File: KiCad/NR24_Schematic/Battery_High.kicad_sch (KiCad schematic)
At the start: 9 parts

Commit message: Back at it
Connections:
- net State_of_Chrg_ANLG: now reaches U?.11 (State_of_Charge(0-5V))
- net Disch_Crnt_Lmt_ANLG: now reaches U?.14 (Discharge_Current_Lim(0-5V))
- net STDWN CT: no longer names the net of U?.15 (Multi_Purpose_Input)
- net STDWN CT: no longer RL1.7
- new net Into Battery AIR Loop: RL1.7
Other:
- note added: "discharge Enable on can"
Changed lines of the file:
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@@
+    (stroke (width 0) (type default))
+  )
+  (wire (pts (xy 118.11 158.75) (xy 81.28 158.75))
     (stroke (width 0) (type default))
   )
@@
     (stroke (width 0) (type default))
   )
+  (wire (pts (xy 85.09 106.68) (xy 85.09 151.13))
+    (stroke (width 0) (type default))
+  )
   (wire (pts (xy 87.63 31.75) (xy 118.11 31.75))
     (stroke (width 1) (type default))
@@
     (stroke (width 0.75) (type default) (color 0 132 132 1))
   )
-  (wire (pts (xy 168.91 135.89) (xy 233.68 135.89))
-    (stroke (width 0) (type default))
-  )
   (wire (pts (xy 209.55 53.34) (xy 233.68 53.34))
     (stroke (width 0) (type default))
@@
     (stroke (width 0) (type default))
   )
+  (wire (pts (xy 196.85 135.89) (xy 233.68 135.89))
+    (stroke (width 0) (type default))
+  )
   (wire (pts (xy 231.14 95.25) (xy 257.81 95.25))
     (stroke (width 0) (type default))
@@
     (stroke (width 1) (type default))
   )
+  (wire (pts (xy 118.11 151.13) (xy 85.09 151.13))
+    (stroke (width 0) (type default))
+  )
   (wire (pts (xy 87.63 38.1) (xy 93.98 38.1))
     (stroke (width 1) (type default))
@@
   (wire (pts (xy 78.74 48.26) (xy 62.23 48.26))
     (stroke (width 1) (type default))
+  )
+  (wire (pts (xy 81.28 106.68) (xy 81.28 158.75))
+    (stroke (width 0) (type default))
   )
   (wire (pts (xy 231.14 113.03) (xy 233.68 113.03))
@@
     (effects (font (size 1.27 1.27)) (justify left bottom))
   )
+  (text "discharge Enable on can" (at 163.83 114.3 0)
+    (effects (font (size 1.27 1.27)) (justify left bottom))
+  )
   (label "CAN_Ground" (at 106.68 116.84 0) (fields_autoplaced)
     (effects (font (size 1.27 1.27)) (justify left bottom))
@@
     (effects (font (size 1.27 1.27)) (justify left bottom))
   )
-  (label "STDWN CT" (at 175.26 135.89 0) (fields_autoplaced)
-    (effects (font (size 1.27 1.27)) (justify left bottom))
+  (label "STDWN CT" (at 196.85 135.89 0) (fields_autoplaced)
+    (effects (font (size 1.27 1.27)) (justify left bottom))
+  )
+  (global_label "Into Battery AIR Loop" (shape input) (at 196.85 135.89 180) (fields_autoplaced)
+    (effects (font (size 1.27 1.27)) (justify right))
+    (property "Intersheetrefs" "${INTERSHEET_REFS}" (at 173.1822 135.89 0)
+      (effects (font (size 1.27 1.27)) (justify right) hide)
+    )
   )
   (hierarchical_label "Charge Sig" (shape input) (at 93.98 106.68 90) (fields_autoplaced)
@@
     (effects (font (size 1.27 1.27)) (justify left))
   )
+  (hierarchical_label "State_of_Chrg_ANLG" (shape input) (at 85.09 106.68 90) (fields_autoplaced)
+    (effects (font (size 1.27 1.27)) (justify left))
+  )
   (hierarchical_label "LV_High" (shape input) (at 97.79 106.68 90) (fields_autoplaced)
     (effects (font (size 1.27 1.27) (thickness 0.254) bold) (justify left))
@@
     (effects (font (size 1.27 1.27)) (justify left))
   )
+  (hierarchical_label "Disch_Crnt_Lmt_ANLG" (shape input) (at 81.28 106.68 90) (fields_autoplaced)
+    (effects (font (size 1.27 1.27)) (justify left))
+  )

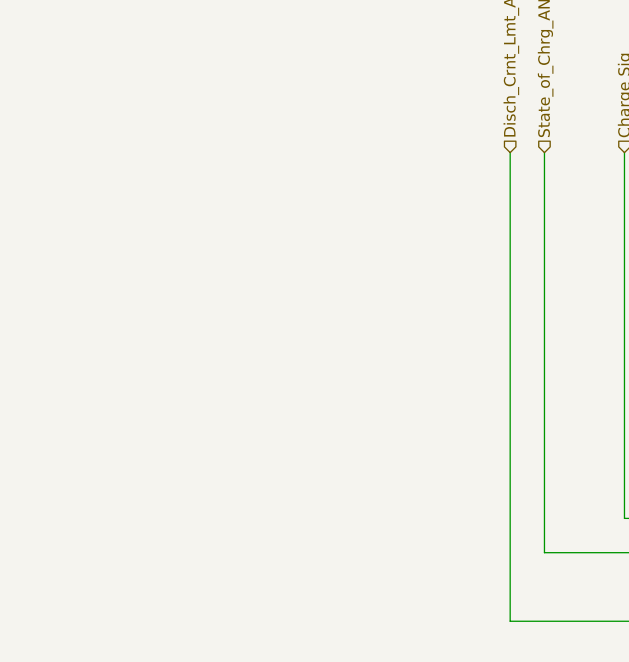
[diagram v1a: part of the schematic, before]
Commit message: added accumulator info
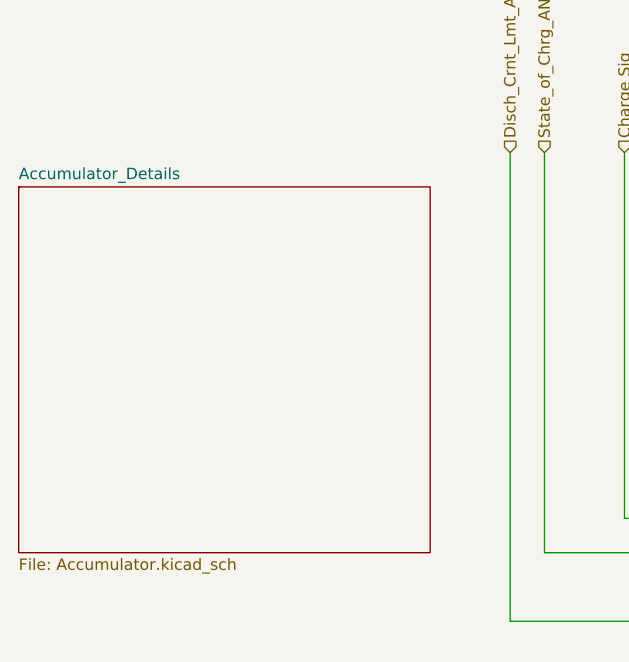
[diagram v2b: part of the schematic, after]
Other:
- added sheet Accumulator_Details (Accumulator.kicad_sch)
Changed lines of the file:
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@@
     (pin "2")
     (instances
-      (project "Car_TractiveSystem_v2"
+      (project "Car_TractiveSystem_MAIN"
         (path "/588b5c14-1813-4e1d-9dbe-940839ecebe3"
           (reference "SW?") (unit 1)
@@
     (pin "8")
     (instances
-      (project "Car_TractiveSystem_v2"
+      (project "Car_TractiveSystem_MAIN"
         (path "/588b5c14-1813-4e1d-9dbe-940839ecebe3"
           (reference "U?") (unit 1)
@@
     (pin "9")
     (instances
-      (project "Car_TractiveSystem_v2"
+      (project "Car_TractiveSystem_MAIN"
         (path "/588b5c14-1813-4e1d-9dbe-940839ecebe3/600c7e11-1cec-4d55-8384-7f41b96b4c2b"
           (reference "RL3") (unit 1)
@@
     (pin "9")
     (instances
-      (project "Car_TractiveSystem_v2"
+      (project "Car_TractiveSystem_MAIN"
         (path "/588b5c14-1813-4e1d-9dbe-940839ecebe3/600c7e11-1cec-4d55-8384-7f41b96b4c2b"
           (reference "RL1") (unit 1)
@@
     (pin "2")
     (instances
-      (project "Car_TractiveSystem_v2"
+      (project "Car_TractiveSystem_MAIN"
         (path "/588b5c14-1813-4e1d-9dbe-940839ecebe3/600c7e11-1cec-4d55-8384-7f41b96b4c2b"
           (reference "D5") (unit 1)
@@
     (pin "2")
     (instances
-      (project "Car_TractiveSystem_v2"
+      (project "Car_TractiveSystem_MAIN"
         (path "/588b5c14-1813-4e1d-9dbe-940839ecebe3"
           (reference "SW?") (unit 1)
@@
     (pin "2")
     (instances
-      (project "Car_TractiveSystem_v2"
+      (project "Car_TractiveSystem_MAIN"
         (path "/588b5c14-1813-4e1d-9dbe-940839ecebe3/600c7e11-1cec-4d55-8384-7f41b96b4c2b"
           (reference "BT4") (unit 1)
@@
     (pin "2")
     (instances
-      (project "Car_TractiveSystem_v2"
+      (project "Car_TractiveSystem_MAIN"
         (path "/588b5c14-1813-4e1d-9dbe-940839ecebe3/600c7e11-1cec-4d55-8384-7f41b96b4c2b"
           (reference "D7") (unit 1)
@@
     (pin "9")
     (instances
-      (project "Car_TractiveSystem_v2"
+      (project "Car_TractiveSystem_MAIN"
         (path "/588b5c14-1813-4e1d-9dbe-940839ecebe3"
           (reference "U?") (unit 1)
@@
       )
     )
+  )
+  (sheet (at 26.67 110.49) (size 45.72 40.64) (fields_autoplaced)
+    (stroke (width 0.1524) (type solid))
+    (fill (color 0 0 0 0.0000))
+    (property "Sheetname" "Accumulator_Details" (at 26.67 109.7784 0)
+      (effects (font (size 1.27 1.27)) (justify left bottom))
+    )
+    (property "Sheetfile" "Accumulator.kicad_sch" (at 26.67 151.7146 0)
+      (effects (font (size 1.27 1.27)) (justify left top))
+    )
+    (instances
+      (project "Car_TractiveSystem_MAIN"
+        (path "/588b5c14-1813-4e1d-9dbe-940839ecebe3/600c7e11-1cec-4d55-8384-7f41b96b4c2b" (page "7"))
+      )
+    )

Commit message: first iteration
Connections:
- net Disch_Crnt_Lmt_ANLG: no longer names the net of U?.14 (Discharge_Current_Lim(0-5V))
- net State_of_Chrg_ANLG: no longer names the net of U?.11 (State_of_Charge(0-5V))
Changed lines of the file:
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@@
-    (stroke (width 0) (type default))
-  )
-  (wire (pts (xy 118.11 158.75) (xy 81.28 158.75))
     (stroke (width 0) (type default))
   )
@@
     (stroke (width 0) (type default))
   )
-  (wire (pts (xy 85.09 106.68) (xy 85.09 151.13))
-    (stroke (width 0) (type default))
-  )
   (wire (pts (xy 87.63 31.75) (xy 118.11 31.75))
     (stroke (width 1) (type default))
@@
     (stroke (width 1) (type default))
   )
-  (wire (pts (xy 118.11 151.13) (xy 85.09 151.13))
-    (stroke (width 0) (type default))
-  )
   (wire (pts (xy 87.63 38.1) (xy 93.98 38.1))
     (stroke (width 1) (type default))
@@
   (wire (pts (xy 78.74 48.26) (xy 62.23 48.26))
     (stroke (width 1) (type default))
-  )
-  (wire (pts (xy 81.28 106.68) (xy 81.28 158.75))
-    (stroke (width 0) (type default))
   )
   (wire (pts (xy 231.14 113.03) (xy 233.68 113.03))
@@
     (effects (font (size 1.27 1.27)) (justify left))
   )
-  (hierarchical_label "State_of_Chrg_ANLG" (shape input) (at 85.09 106.68 90) (fields_autoplaced)
-    (effects (font (size 1.27 1.27)) (justify left))
-  )
   (hierarchical_label "LV_High" (shape input) (at 97.79 106.68 90) (fields_autoplaced)
     (effects (font (size 1.27 1.27) (thickness 0.254) bold) (justify left))
@@
     (effects (font (size 1.27 1.27)) (justify left))
   )
-  (hierarchical_label "Disch_Crnt_Lmt_ANLG" (shape input) (at 81.28 106.68 90) (fields_autoplaced)
-    (effects (font (size 1.27 1.27)) (justify left))
-  )

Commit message: Pre Break Schematic
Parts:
- renumbered BT4 to BT1, D5 to D4, D7 to D5, RL3 to RL1, RL1 to RL2
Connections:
- net AMS Fault: no longer names the net of RL2.9, SW?.1 (A), U?.9 (Multi_Purpose_Output_1)
- net CAN_Ground renamed CAN_GND
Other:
- note added: "AMS Fault"
- note added: "CAN_GND"
- note added: "CAN_High"
- note added: "CAN_Low"
- note added: "SHTDWN CRCT"
